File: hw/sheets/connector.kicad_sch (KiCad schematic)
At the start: 1 part, among them J1 AH58893-T9B10-3F

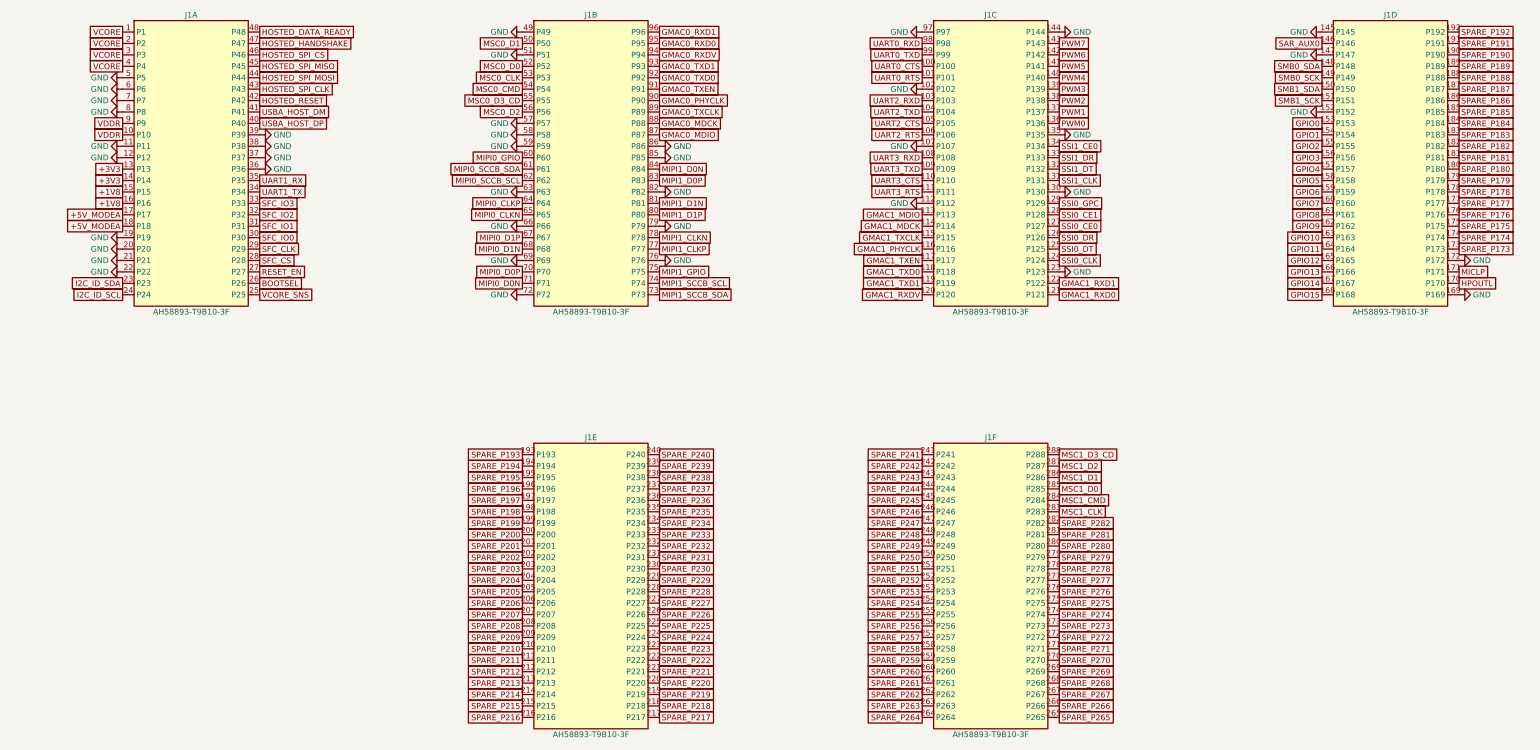
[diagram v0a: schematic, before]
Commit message: Fix schematic<->PCB linking, reorder J1 pins by connected peer, add +3V3 plane, wire microSD card-detect
- schgen.py: deterministic per-symbol UUIDs (uuid5, keyed on ref designator)
  instead of random uuid4, so PCB footprints stay linked to their schematic
  symbol across regenerations; link all 133 real PCB footprints to their
  schematic symbol via path, fixing "Update PCB from Schematic" placing
  duplicates.
- J1 pin reorg: audio (HPOUTL/MICLP) moved from 170/171 to 6/7 (170/171 now
  GND); USBA_HOST_DP/DM moved from 40/41 to 20/21 (40/41 now GND); the 20
  pins connected directly to U8 (ESP32-S3) reordered so U8's ascending pin
  number maps to J1's descending pin number; +5V_MODEA (redundant -- a
  self-contained module already needs its own bare-bench power input)
  replaced with +5V_SW (the real arbitrated switched-5V rail) on pins 17/18.
- New +3V3 copper pour on In1.Cu, mirroring the existing GND pour; every
  +3V3 pad on the board (38, now 39 with R43) gets a stub trace + via down
  to it.
- microSD (J4): switched to the Micro_SD_Card_Det2 symbol so pin 10 (the
  footprint's real card-detect pad) has somewhere to attach; added R43
  (1M, matches TeaCup 3.3's R22) pulling MSC0_CD up to +3V3.
- fp-lib-table: replaced hardcoded /usr/share/kicad/footprints/... paths
  with ${KICAD10_FOOTPRINT_DIR}, fixing "footprint not found" errors for
  every component when Update PCB from Schematic runs outside this Linux
  environment.

Verified throughout via isolated ERC/DRC diffs against pre-change
baselines; each change confirmed to produce only its own intended delta.
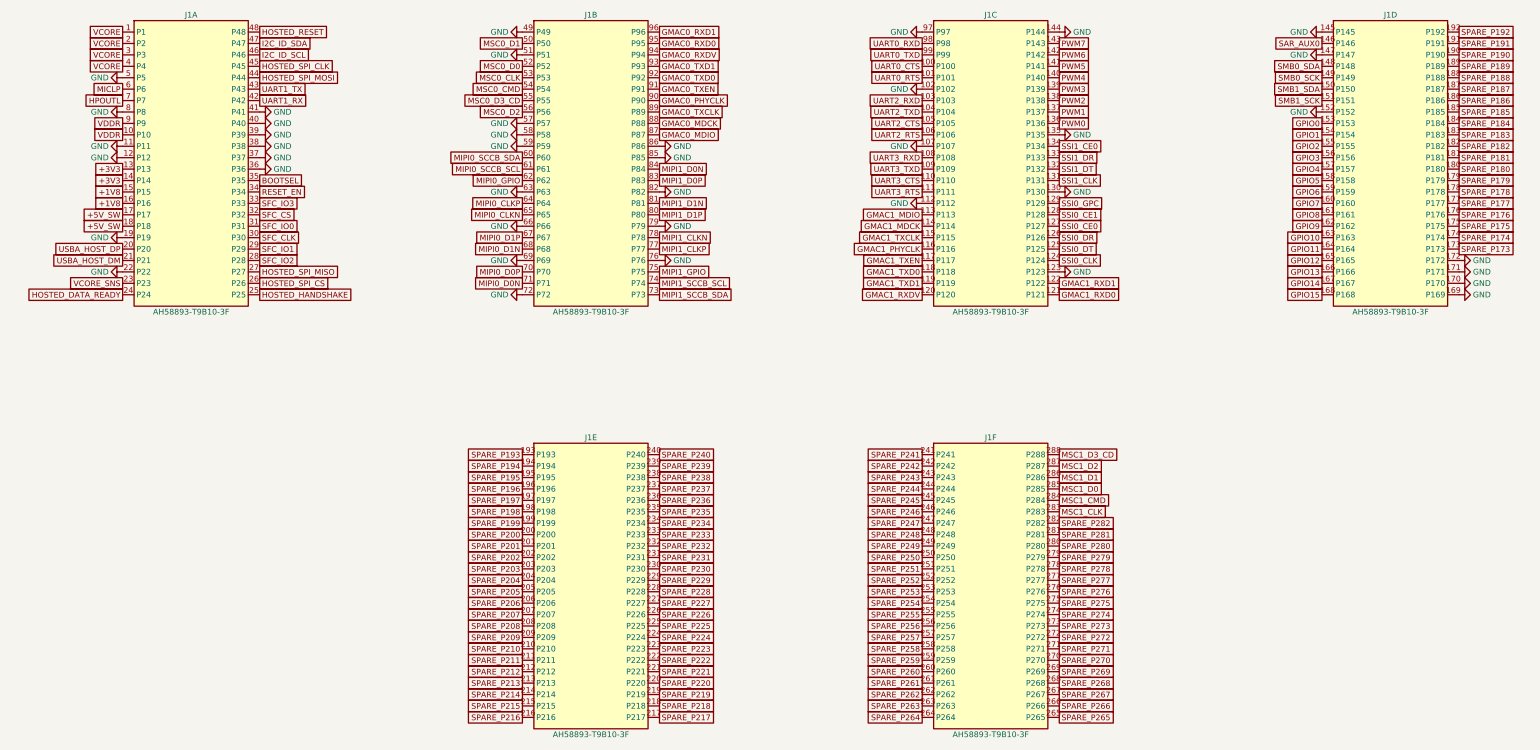
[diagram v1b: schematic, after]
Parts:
- removed unit 1 of J1
- removed unit 2 of J1
- removed unit 4 of J1
- removed unit 3 of J1
- removed unit 5 of J1
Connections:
- net +1V8: now also J1.15 (P15), J1.16 (P16)
- net +3V3: now also J1.13 (P13), J1.14 (P14)
- net BOOTSEL: now also J1.35 (P35)
- net GMAC0_MDCK: now also J1.88 (P88)
- net GMAC0_MDIO: now also J1.87 (P87)
- net GMAC0_PHYCLK: now also J1.90 (P90)
- net GMAC0_RXD0: now also J1.95 (P95)
- net GMAC0_RXD1: now also J1.96 (P96)
- net GMAC0_RXDV: now also J1.94 (P94)
- net GMAC0_TXCLK: now also J1.89 (P89)
- net GMAC0_TXD0: now also J1.92 (P92)
- net GMAC0_TXD1: now also J1.93 (P93)
- net GMAC0_TXEN: now also J1.91 (P91)
- net GMAC1_MDCK: now also J1.114 (P114)
- net GMAC1_MDIO: now also J1.113 (P113)
- net GMAC1_PHYCLK: now also J1.116 (P116)
- net GMAC1_RXD0: now also J1.121 (P121)
- net GMAC1_RXD1: now also J1.122 (P122)
- net GMAC1_RXDV: now also J1.120 (P120)
- net GMAC1_TXCLK: now also J1.115 (P115)
- net GMAC1_TXD0: now also J1.118 (P118)
- net GMAC1_TXD1: now also J1.119 (P119)
- net GMAC1_TXEN: now also J1.117 (P117)
- net GND: now also J1.102 (P102), J1.107 (P107), J1.11 (P11), J1.112 (P112), J1.12 (P12), J1.123 (P123), J1.130 (P130), J1.135 (P135), J1.144 (P144), J1.145 (P145), J1.147 (P147), J1.152 (P152), J1.169 (P169), J1.170 (P170), J1.171 (P171), J1.172 (P172), J1.19 (P19), J1.22 (P22), J1.36 (P36), J1.37 (P37), J1.38 (P38), J1.39 (P39), J1.40 (P40), J1.41 (P41), J1.49 (P49), J1.5 (P5), J1.51 (P51), J1.57 (P57), J1.58 (P58), J1.59 (P59), J1.63 (P63), J1.66 (P66), J1.69 (P69), J1.72 (P72), J1.76 (P76), J1.79 (P79), J1.8 (P8), J1.82 (P82), J1.85 (P85), J1.86 (P86), J1.97 (P97)
- net GPIO0: now also J1.153 (P153)
- net GPIO1: now also J1.154 (P154)
- net GPIO10: now also J1.163 (P163)
- net GPIO11: now also J1.164 (P164)
- net GPIO12: now also J1.165 (P165)
- net GPIO13: now also J1.166 (P166)
- net GPIO14: now also J1.167 (P167)
- net GPIO15: now also J1.168 (P168)
- net GPIO2: now also J1.155 (P155)
- net GPIO3: now also J1.156 (P156)
- net GPIO4: now also J1.157 (P157)
- net GPIO5: now also J1.158 (P158)
- net GPIO6: now also J1.159 (P159)
- net GPIO7: now also J1.160 (P160)
- net GPIO8: now also J1.161 (P161)
- net GPIO9: now also J1.162 (P162)
- net HOSTED_DATA_READY: now also J1.24 (P24)
- net HOSTED_HANDSHAKE: now also J1.25 (P25)
- net HOSTED_RESET: now also J1.48 (P48)
- net HOSTED_SPI_CLK: now also J1.45 (P45)
- net HOSTED_SPI_CS: now also J1.26 (P26)
- net HOSTED_SPI_MISO: now also J1.27 (P27)
- net HOSTED_SPI_MOSI: now also J1.44 (P44)
- net HPOUTL: now also J1.7 (P7)
- net I2C_ID_SCL: now also J1.46 (P46)
- net I2C_ID_SDA: now also J1.47 (P47)
- net MICLP: now also J1.6 (P6)
- net MIPI0_CLKN: now also J1.65 (P65)
- net MIPI0_CLKP: now also J1.64 (P64)
- net MIPI0_D0N: now also J1.71 (P71)
- net MIPI0_D0P: now also J1.70 (P70)
- net MIPI0_D1N: now also J1.68 (P68)
- net MIPI0_D1P: now also J1.67 (P67)
- net MIPI0_GPIO: now also J1.62 (P62)
- net MIPI0_SCCB_SCL: now also J1.61 (P61)
- net MIPI0_SCCB_SDA: now also J1.60 (P60)
- net MIPI1_CLKN: now also J1.78 (P78)
- net MIPI1_CLKP: now also J1.77 (P77)
- net MIPI1_D0N: now also J1.84 (P84)
- net MIPI1_D0P: now also J1.83 (P83)
- net MIPI1_D1N: now also J1.81 (P81)
- net MIPI1_D1P: now also J1.80 (P80)
- net MIPI1_GPIO: now also J1.75 (P75)
- net MIPI1_SCCB_SCL: now also J1.74 (P74)
- net MIPI1_SCCB_SDA: now also J1.73 (P73)
- net MSC0_CLK: now also J1.53 (P53)
- net MSC0_CMD: now also J1.54 (P54)
- net MSC0_D0: now also J1.52 (P52)
- net MSC0_D1: now also J1.50 (P50)
- net MSC0_D2: now also J1.56 (P56)
- net MSC0_D3_CD: now also J1.55 (P55)
- net PWM0: now also J1.136 (P136)
- net PWM1: now also J1.137 (P137)
- net PWM2: now also J1.138 (P138)
- net PWM3: now also J1.139 (P139)
- net PWM4: now also J1.140 (P140)
- net PWM5: now also J1.141 (P141)
- net PWM6: now also J1.142 (P142)
- net PWM7: now also J1.143 (P143)
- net RESET_EN: now also J1.34 (P34)
- net SAR_AUX0: now also J1.146 (P146)
- net SFC_CLK: now also J1.30 (P30)
- net SFC_CS: now also J1.32 (P32)
- net SFC_IO0: now also J1.31 (P31)
- net SFC_IO1: now also J1.29 (P29)
- net SFC_IO2: now also J1.28 (P28)
- net SFC_IO3: now also J1.33 (P33)
- net SMB0_SCK: now also J1.149 (P149)
- net SMB0_SDA: now also J1.148 (P148)
- net SMB1_SCK: now also J1.151 (P151)
- net SMB1_SDA: now also J1.150 (P150)
- net SPARE_P173: now also J1.173 (P173)
- net SPARE_P174: now also J1.174 (P174)
- net SPARE_P175: now also J1.175 (P175)
- net SPARE_P176: now also J1.176 (P176)
- net SPARE_P177: now also J1.177 (P177)
- net SPARE_P178: now also J1.178 (P178)
- net SPARE_P179: now also J1.179 (P179)
- net SPARE_P180: now also J1.180 (P180)
- net SPARE_P181: now also J1.181 (P181)
- net SPARE_P182: now also J1.182 (P182)
- net SPARE_P183: now also J1.183 (P183)
- net SPARE_P184: now also J1.184 (P184)
- net SPARE_P185: now also J1.185 (P185)
- net SPARE_P186: now also J1.186 (P186)
- net SPARE_P187: now also J1.187 (P187)
- net SPARE_P188: now also J1.188 (P188)
- net SPARE_P189: now also J1.189 (P189)
- net SPARE_P190: now also J1.190 (P190)
- net SPARE_P191: now also J1.191 (P191)
- net SPARE_P192: now also J1.192 (P192)
- net SPARE_P193: now also J1.193 (P193)
- net SPARE_P194: now also J1.194 (P194)
- net SPARE_P195: now also J1.195 (P195)
- net SPARE_P196: now also J1.196 (P196)
- net SPARE_P197: now also J1.197 (P197)
- net SPARE_P198: now also J1.198 (P198)
- net SPARE_P199: now also J1.199 (P199)
- net SPARE_P200: now also J1.200 (P200)
- net SPARE_P201: now also J1.201 (P201)
- net SPARE_P202: now also J1.202 (P202)
- net SPARE_P203: now also J1.203 (P203)
- net SPARE_P204: now also J1.204 (P204)
- net SPARE_P205: now also J1.205 (P205)
- net SPARE_P206: now also J1.206 (P206)
- net SPARE_P207: now also J1.207 (P207)
- net SPARE_P208: now also J1.208 (P208)
- net SPARE_P209: now also J1.209 (P209)
- net SPARE_P210: now also J1.210 (P210)
- net SPARE_P211: now also J1.211 (P211)
- net SPARE_P212: now also J1.212 (P212)
- net SPARE_P213: now also J1.213 (P213)
- net SPARE_P214: now also J1.214 (P214)
- net SPARE_P215: now also J1.215 (P215)
- net SPARE_P216: now also J1.216 (P216)
- net SPARE_P217: now also J1.217 (P217)
- net SPARE_P218: now also J1.218 (P218)
- net SPARE_P219: now also J1.219 (P219)
- net SPARE_P220: now also J1.220 (P220)
- net SPARE_P221: now also J1.221 (P221)
- net SPARE_P222: now also J1.222 (P222)
- net SPARE_P223: now also J1.223 (P223)
- net SPARE_P224: now also J1.224 (P224)
- net SPARE_P225: now also J1.225 (P225)
- net SPARE_P226: now also J1.226 (P226)
- net SPARE_P227: now also J1.227 (P227)
- net SPARE_P228: now also J1.228 (P228)
- net SPARE_P229: now also J1.229 (P229)
- net SPARE_P230: now also J1.230 (P230)
- net SPARE_P231: now also J1.231 (P231)
- net SPARE_P232: now also J1.232 (P232)
- net SPARE_P233: now also J1.233 (P233)
- net SPARE_P234: now also J1.234 (P234)
- net SPARE_P235: now also J1.235 (P235)
- net SPARE_P236: now also J1.236 (P236)
- net SPARE_P237: now also J1.237 (P237)
- net SPARE_P238: now also J1.238 (P238)
- net SPARE_P239: now also J1.239 (P239)
- net SPARE_P240: now also J1.240 (P240)
- net SSI0_CE0: now also J1.127 (P127)
- net SSI0_CE1: now also J1.128 (P128)
- net SSI0_CLK: now also J1.124 (P124)
- net SSI0_DR: now also J1.126 (P126)
- net SSI0_DT: now also J1.125 (P125)
- net SSI0_GPC: now also J1.129 (P129)
- net SSI1_CE0: now also J1.134 (P134)
- net SSI1_CLK: now also J1.131 (P131)
- net SSI1_DR: now also J1.133 (P133)
- net SSI1_DT: now also J1.132 (P132)
- net UART0_CTS: now also J1.100 (P100)
- net UART0_RTS: now also J1.101 (P101)
- net UART0_RXD: now also J1.98 (P98)
- net UART0_TXD: now also J1.99 (P99)
- net UART1_RX: now also J1.42 (P42)
- net UART1_TX: now also J1.43 (P43)
- net UART2_CTS: now also J1.105 (P105)
- net UART2_RTS: now also J1.106 (P106)
- net UART2_RXD: now also J1.103 (P103)
- net UART2_TXD: now also J1.104 (P104)
- net UART3_CTS: now also J1.110 (P110)
- net UART3_RTS: now also J1.111 (P111)
- net UART3_RXD: now also J1.108 (P108)
- net UART3_TXD: now also J1.109 (P109)
- net USBA_HOST_DM: now also J1.21 (P21)
- net USBA_HOST_DP: now also J1.20 (P20)
- net VCORE: now also J1.1 (P1), J1.2 (P2), J1.3 (P3), J1.4 (P4)
- net VCORE_SNS: now also J1.23 (P23)
- net VDDR: now also J1.10 (P10), J1.9 (P9)
- new net +5V_SW: J1.17 (P17), J1.18 (P18)
